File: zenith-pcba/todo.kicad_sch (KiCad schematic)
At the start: 1 part, among them U2 K4B4G1646E-BCNB

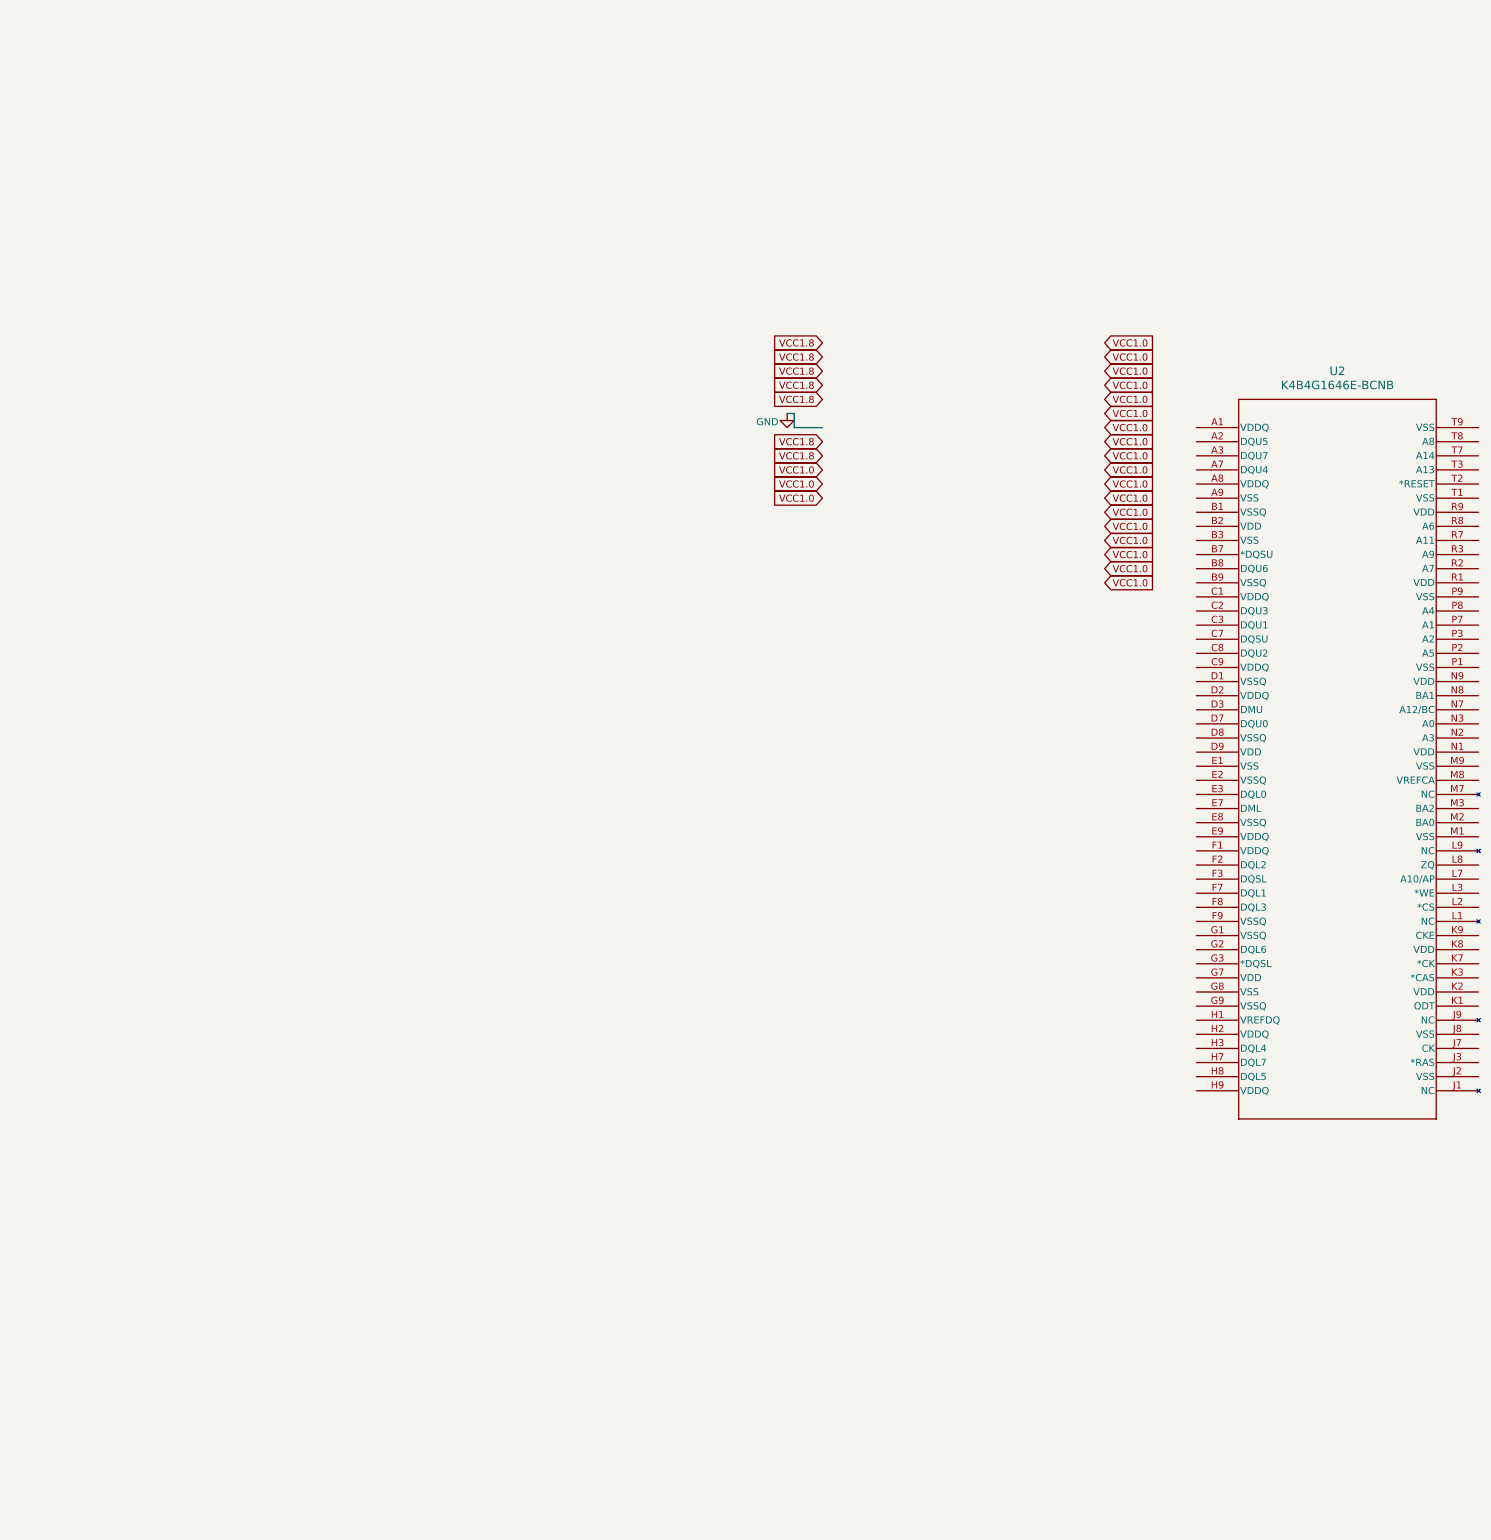
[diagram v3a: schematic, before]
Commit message: feat(hardware): ddr3 sodimm import
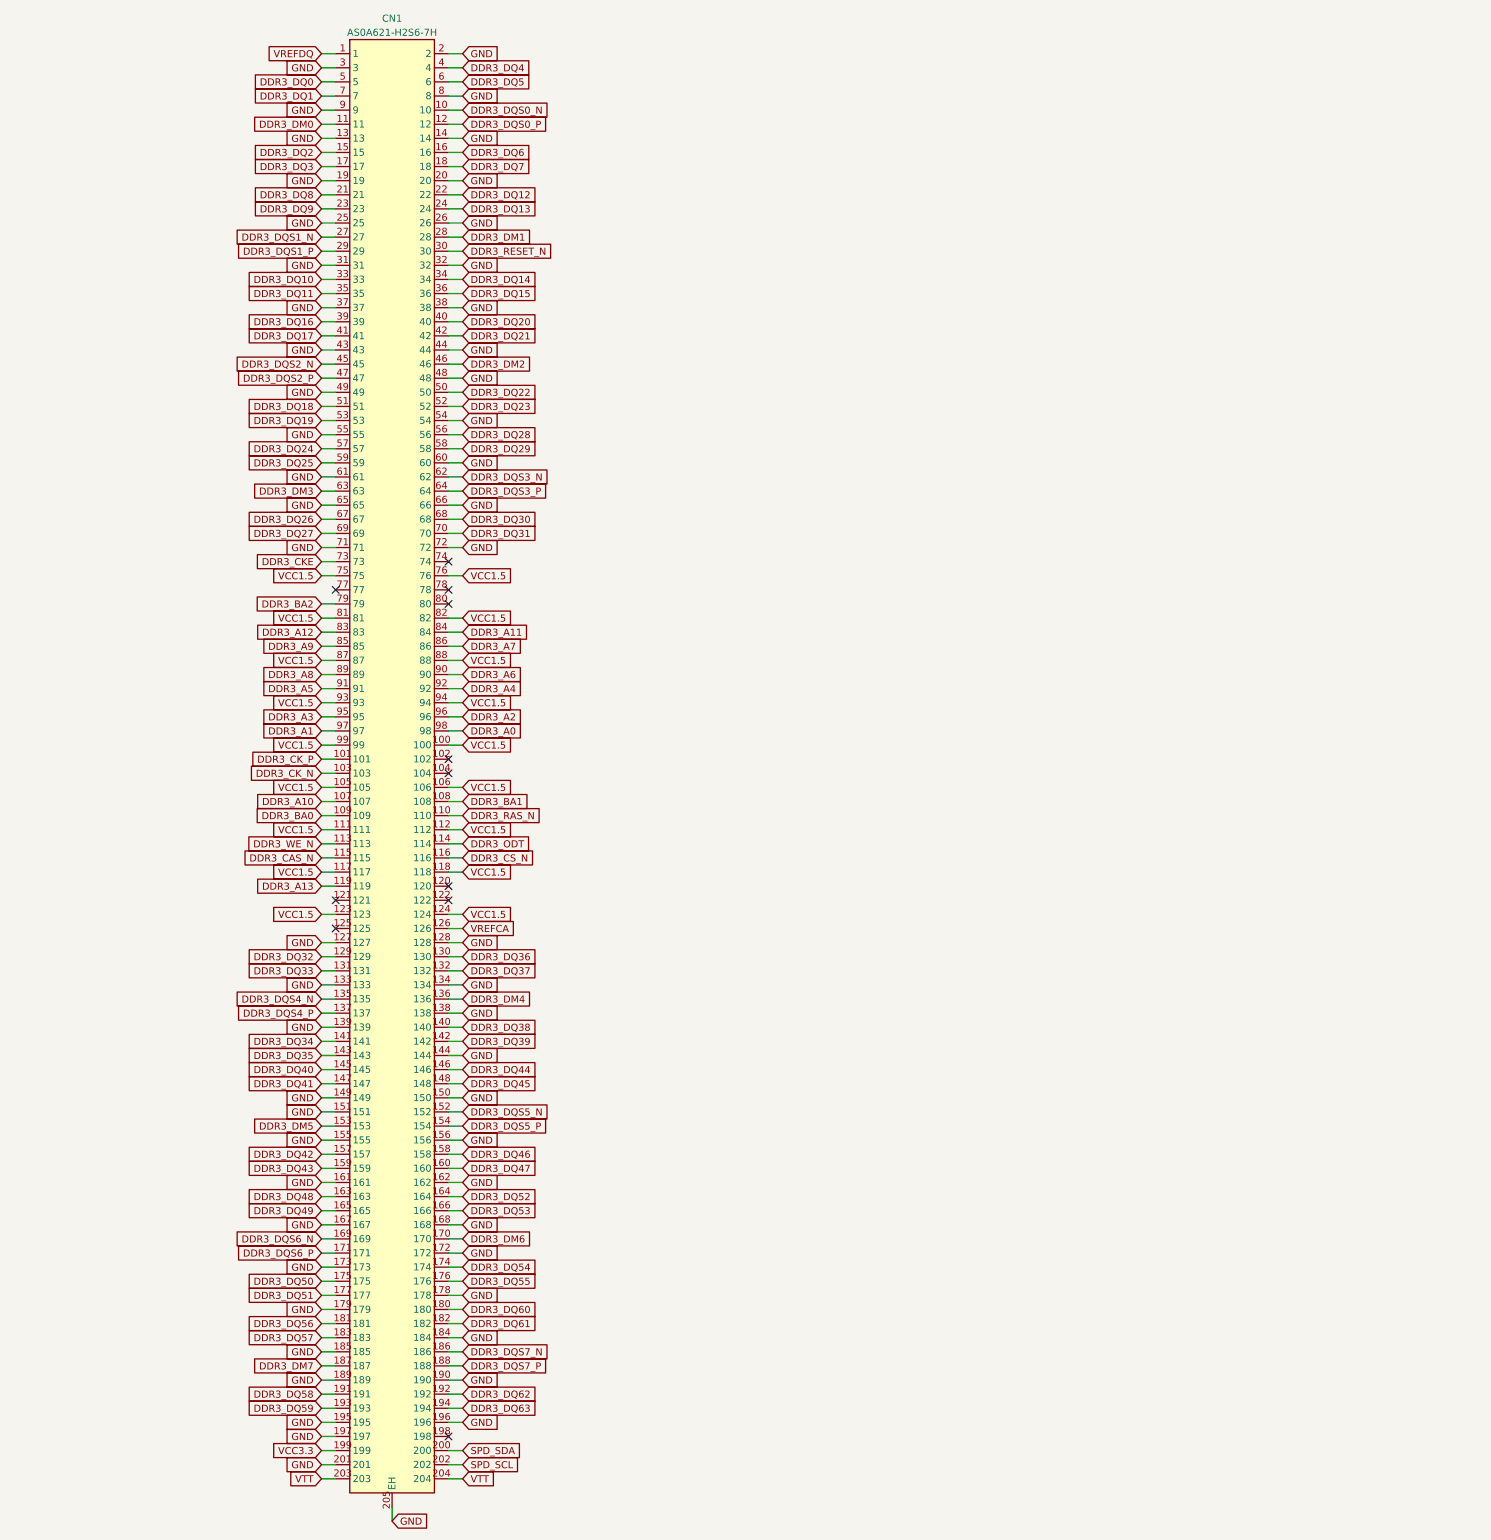
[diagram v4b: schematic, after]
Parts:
- removed U2: K4B4G1646E-BCNB, BGA96_K4B4G1_SAM, symbol K4B4G1646E-BCNB:K4B4G1646E-BCNB
- added CN1: AS0A621-H2S6-7H, easyeda2kicad:CONN-SMD_204P-P0.60_AS0A621-H2S6-7H, symbol easyeda2kicad:AS0A621-H2S6-7H
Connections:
- net GND: now also CN1.127, CN1.128, CN1.13, CN1.133, CN1.134, CN1.138, CN1.139, CN1.14, CN1.144, CN1.149, CN1.150, CN1.151, CN1.155, CN1.156, CN1.161, CN1.162, CN1.167, CN1.168, CN1.172, CN1.173, CN1.178, CN1.179, CN1.184, CN1.185, CN1.189, CN1.19, CN1.190, CN1.195, CN1.196, CN1.197, CN1.2, CN1.20, CN1.201, CN1.205 (EH), CN1.25, CN1.26, CN1.3, CN1.31, CN1.32, CN1.37, CN1.38, CN1.43, CN1.44, CN1.48, CN1.49, CN1.54, CN1.55, CN1.60, CN1.61, CN1.65, CN1.66, CN1.71, CN1.72, CN1.8, CN1.9
- new net DDR3_A0: CN1.98
- new net DDR3_A1: CN1.97
- new net DDR3_A10: CN1.107
- new net DDR3_A11: CN1.84
- new net DDR3_A12: CN1.83
- new net DDR3_A13: CN1.119
- new net DDR3_A2: CN1.96
- new net DDR3_A3: CN1.95
- new net DDR3_A4: CN1.92
- new net DDR3_A5: CN1.91
- new net DDR3_A6: CN1.90
- new net DDR3_A7: CN1.86
- new net DDR3_A8: CN1.89
- new net DDR3_A9: CN1.85
- new net DDR3_BA0: CN1.109
- new net DDR3_BA1: CN1.108
- new net DDR3_BA2: CN1.79
- new net DDR3_CAS_N: CN1.115
- new net DDR3_CKE: CN1.73
- new net DDR3_CK_N: CN1.103
- new net DDR3_CK_P: CN1.101
- new net DDR3_CS_N: CN1.116
- new net DDR3_DM0: CN1.11
- new net DDR3_DM1: CN1.28
- new net DDR3_DM2: CN1.46
- new net DDR3_DM3: CN1.63
- new net DDR3_DM4: CN1.136
- new net DDR3_DM5: CN1.153
- new net DDR3_DM6: CN1.170
- new net DDR3_DM7: CN1.187
- new net DDR3_DQ0: CN1.5
- new net DDR3_DQ1: CN1.7
- new net DDR3_DQ10: CN1.33
- new net DDR3_DQ11: CN1.35
- new net DDR3_DQ12: CN1.22
- new net DDR3_DQ13: CN1.24
- new net DDR3_DQ14: CN1.34
- new net DDR3_DQ15: CN1.36
- new net DDR3_DQ16: CN1.39
- new net DDR3_DQ17: CN1.41
- new net DDR3_DQ18: CN1.51
- new net DDR3_DQ19: CN1.53
- new net DDR3_DQ2: CN1.15
- new net DDR3_DQ20: CN1.40
- new net DDR3_DQ21: CN1.42
- new net DDR3_DQ22: CN1.50
- new net DDR3_DQ23: CN1.52
- new net DDR3_DQ24: CN1.57
- new net DDR3_DQ25: CN1.59
- new net DDR3_DQ26: CN1.67
- new net DDR3_DQ27: CN1.69
- new net DDR3_DQ28: CN1.56
- new net DDR3_DQ29: CN1.58
- new net DDR3_DQ3: CN1.17
- new net DDR3_DQ30: CN1.68
- new net DDR3_DQ31: CN1.70
- new net DDR3_DQ32: CN1.129
- new net DDR3_DQ33: CN1.131
- new net DDR3_DQ34: CN1.141
- new net DDR3_DQ35: CN1.143
- new net DDR3_DQ36: CN1.130
- new net DDR3_DQ37: CN1.132
- new net DDR3_DQ38: CN1.140
- new net DDR3_DQ39: CN1.142
- new net DDR3_DQ4: CN1.4
- new net DDR3_DQ40: CN1.145
- new net DDR3_DQ41: CN1.147
- new net DDR3_DQ42: CN1.157
- new net DDR3_DQ43: CN1.159
- new net DDR3_DQ44: CN1.146
- new net DDR3_DQ45: CN1.148
- new net DDR3_DQ46: CN1.158
- new net DDR3_DQ47: CN1.160
- new net DDR3_DQ48: CN1.163
- new net DDR3_DQ49: CN1.165
- new net DDR3_DQ5: CN1.6
- new net DDR3_DQ50: CN1.175
- new net DDR3_DQ51: CN1.177
- new net DDR3_DQ52: CN1.164
- new net DDR3_DQ53: CN1.166
- new net DDR3_DQ54: CN1.174
- new net DDR3_DQ55: CN1.176
- new net DDR3_DQ56: CN1.181
- new net DDR3_DQ57: CN1.183
- new net DDR3_DQ58: CN1.191
- new net DDR3_DQ59: CN1.193
- new net DDR3_DQ6: CN1.16
- new net DDR3_DQ60: CN1.180
- new net DDR3_DQ61: CN1.182
- new net DDR3_DQ62: CN1.192
- new net DDR3_DQ63: CN1.194
- new net DDR3_DQ7: CN1.18
- new net DDR3_DQ8: CN1.21
- new net DDR3_DQ9: CN1.23
- new net DDR3_DQS0_N: CN1.10
- new net DDR3_DQS0_P: CN1.12
- new net DDR3_DQS1_N: CN1.27
- new net DDR3_DQS1_P: CN1.29
- new net DDR3_DQS2_N: CN1.45
- new net DDR3_DQS2_P: CN1.47
- new net DDR3_DQS3_N: CN1.62
- new net DDR3_DQS3_P: CN1.64
- new net DDR3_DQS4_N: CN1.135
- new net DDR3_DQS4_P: CN1.137
- new net DDR3_DQS5_N: CN1.152
- new net DDR3_DQS5_P: CN1.154
- new net DDR3_DQS6_N: CN1.169
- new net DDR3_DQS6_P: CN1.171
- new net DDR3_DQS7_N: CN1.186
- new net DDR3_DQS7_P: CN1.188
- new net DDR3_ODT: CN1.114
- new net DDR3_RAS_N: CN1.110
- new net DDR3_RESET_N: CN1.30
- new net DDR3_WE_N: CN1.113
- new net SPD_SCL: CN1.202
- new net SPD_SDA: CN1.200
- new net VCC1.5: CN1.100, CN1.105, CN1.106, CN1.111, CN1.112, CN1.117, CN1.118, CN1.123, CN1.124, CN1.75, CN1.76, CN1.81, CN1.82, CN1.87, CN1.88, CN1.93, CN1.94, CN1.99
- new net VCC3.3: CN1.199
- new net VREFCA: CN1.126
- new net VREFDQ: CN1.1
- new net VTT: CN1.203, CN1.204
- no-connect marks 0 -> 11
